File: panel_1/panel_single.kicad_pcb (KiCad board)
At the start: 2 copper layers, 20 x 128.5 mm, 8 parts

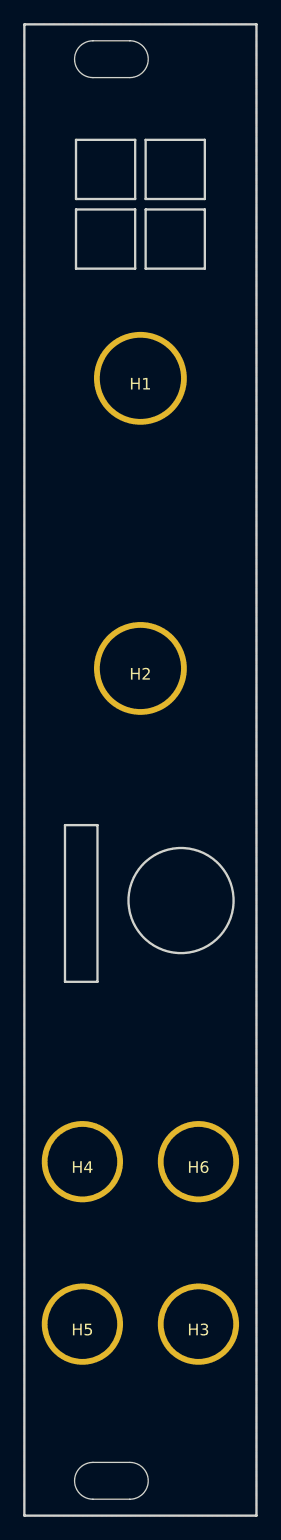
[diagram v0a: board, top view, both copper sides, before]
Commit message: :bug: Fix panel single (better clearance for LEDs & switch)
same
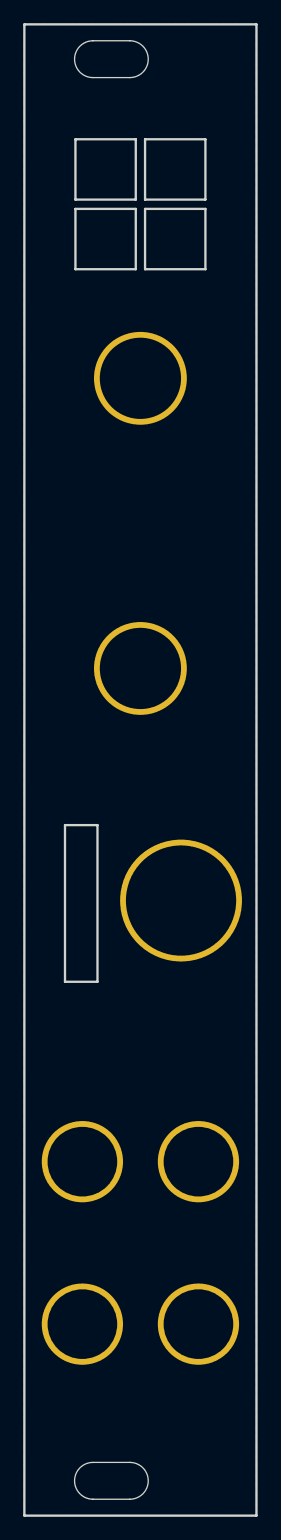
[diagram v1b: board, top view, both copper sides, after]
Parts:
- added H7: MountingHole_Pad, MountingHole:MountingHole_6mm_Pad, F.Cu at (53.5, 105.5)
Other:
- outline, holes or cut-outs redrawn
- board text added: "5mm square holes with .2 mm tolerance"
- board text removed: "5mm square holes with .1 mm tolerance"
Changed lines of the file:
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@@
   (general
     (thickness 1.6)
-    (drawings 85)
+    (drawings 84)
     (tracks 0)
     (zones 0)
-    (modules 8)
+    (modules 9)
     (nets 2)
   )
@@
     (38 B.Mask user)
     (39 F.Mask user)
-    (40 Dwgs.User user)
+    (40 Dwgs.User user hide)
     (41 Cmts.User user)
     (42 Eco1.User user)
@@
     (last_trace_width 0.25)
     (trace_clearance 0.2)
-    (zone_clearance 0.508)
+    (zone_clearance 0)
     (zone_45_only no)
     (trace_min 0.2)
@@
     (mod_text_size 1 1)
     (mod_text_width 0.15)
-    (pad_size 1.524 1.524)
-    (pad_drill 0.762)
+    (pad_size 10.5 10.5)
+    (pad_drill 9.5)
     (pad_to_mask_clearance 0.051)
     (solder_mask_min_width 0.25)
@@
     (add_net GND)
   )
+  (module MountingHole:MountingHole_6mm_Pad (layer F.Cu)
+    (at 53.5 105.5)
+    (descr "Mounting Hole 6mm")
+    (tags "mounting hole 6mm")
+    (attr virtual)
+    (fp_text reference H7 (at 0 -7) (layer F.SilkS) hide
+      (effects (font (size 1 1) (thickness 0.15)))
+    )
+    (fp_text value MountingHole_Pad (at 0 7) (layer F.Fab)
+      (effects (font (size 1 1) (thickness 0.15)))
+    )
+    (fp_circle (center 0 0) (end 6.25 0) (layer F.CrtYd) (width 0.05))
+    (fp_circle (center 0 0) (end 6 0) (layer Cmts.User) (width 0.15))
+    (fp_text user %R (at 22.185 -0.251) (layer F.Fab)
+      (effects (font (size 1 1) (thickness 0.15)))
+    )
+    (pad 1 thru_hole circle (at 0 0) (size 10.5 10.5) (drill 9.5) (layers *.Cu *.Mask)
+      (net 1 GND))
+  )
   (module 4ms-footprints:Rail-mount-slot (layer F.Cu)
     (at 47.5 33)
@@
   (module prok_smd:Alpha_pot_hole_metallized (layer F.Cu)
     (at 50 60.5)
-    (fp_text reference H1 (at 0 0.5) (layer F.SilkS)
+    (fp_text reference H1 (at 0 0.5) (layer F.SilkS) hide
       (effects (font (size 1 1) (thickness 0.15)))
     )
@@
   (module prok_smd:Alpha_pot_hole_metallized (layer F.Cu)
     (at 50 85.5)
-    (fp_text reference H2 (at 0 0.5) (layer F.SilkS)
+    (fp_text reference H2 (at 0 0.5) (layer F.SilkS) hide
       (effects (font (size 1 1) (thickness 0.15)))
     )
@@
   (module prok_smd:thonkiconn_hole_metallized (layer F.Cu)
     (at 55 142)
-    (fp_text reference H3 (at 0 0.5) (layer F.SilkS)
+    (fp_text reference H3 (at 0 0.5) (layer F.SilkS) hide
       (effects (font (size 1 1) (thickness 0.15)))
     )
@@
   (module prok_smd:thonkiconn_hole_metallized (layer F.Cu)
     (at 45 128)
-    (fp_text reference H4 (at 0 0.5) (layer F.SilkS)
+    (fp_text reference H4 (at 0 0.5) (layer F.SilkS) hide
       (effects (font (size 1 1) (thickness 0.15)))
     )
@@
   (module prok_smd:thonkiconn_hole_metallized (layer F.Cu)
     (at 45 142)
-    (fp_text reference H5 (at 0 0.5) (layer F.SilkS)
+    (fp_text reference H5 (at 0 0.5) (layer F.SilkS) hide
       (effects (font (size 1 1) (thickness 0.15)))
     )
@@
   (module prok_smd:thonkiconn_hole_metallized (layer F.Cu)
     (at 55 128)
-    (fp_text reference H6 (at 0 0.5) (layer F.SilkS)
+    (fp_text reference H6 (at 0 0.5) (layer F.SilkS) hide
       (effects (font (size 1 1) (thickness 0.15)))
     )
@@
       (net 1 GND))
   )
-  (gr_text "5mm square holes\nwith .1 mm tolerance" (at 50.2 38.45) (layer Dwgs.User)
+  (gr_line (start 50.5 51) (end 50.5 46) (layer Dwgs.User) (width 0.2))
+  (gr_line (start 44.5 51) (end 44.5 46) (layer Dwgs.User) (width 0.2))
+  (gr_line (start 50.5 45) (end 50.5 40) (layer Dwgs.User) (width 0.2))
+  (gr_line (start 55.5 51) (end 50.5 51) (layer Dwgs.User) (width 0.2))
+  (gr_line (start 49.5 51) (end 44.5 51) (layer Dwgs.User) (width 0.2))
+  (gr_line (start 55.5 45) (end 50.5 45) (layer Dwgs.User) (width 0.2))
+  (gr_line (start 50.5 46) (end 55.5 46) (layer Dwgs.User) (width 0.2))
+  (gr_line (start 44.5 46) (end 49.5 46) (layer Dwgs.User) (width 0.2))
+  (gr_line (start 50.5 40) (end 55.5 40) (layer Dwgs.User) (width 0.2))
+  (gr_line (start 55.5 46) (end 55.5 51) (layer Dwgs.User) (width 0.2))
+  (gr_line (start 49.5 46) (end 49.5 51) (layer Dwgs.User) (width 0.2))
+  (gr_line (start 55.5 40) (end 55.5 45) (layer Dwgs.User) (width 0.2))
+  (gr_line (start 55.6 51.1) (end 50.4 51.1) (layer Edge.Cuts) (width 0.2))
+  (gr_line (start 49.6 51.1) (end 44.4 51.1) (layer Edge.Cuts) (width 0.2))
+  (gr_line (start 55.6 45.1) (end 50.4 45.1) (layer Edge.Cuts) (width 0.2))
+  (gr_line (start 50.4 51.1) (end 50.4 45.9) (layer Edge.Cuts) (width 0.2))
+  (gr_line (start 44.4 51.1) (end 44.4 45.9) (layer Edge.Cuts) (width 0.2))
+  (gr_line (start 50.4 45.1) (end 50.4 39.9) (layer Edge.Cuts) (width 0.2))
+  (gr_line (start 50.4 45.9) (end 55.6 45.9) (layer Edge.Cuts) (width 0.2))
+  (gr_line (start 44.4 45.9) (end 49.6 45.9) (layer Edge.Cuts) (width 0.2))
+  (gr_line (start 50.4 39.9) (end 55.6 39.9) (layer Edge.Cuts) (width 0.2))
+  (gr_line (start 55.6 45.9) (end 55.6 51.1) (layer Edge.Cuts) (width 0.2))
+  (gr_line (start 49.6 45.9) (end 49.6 51.1) (layer Edge.Cuts) (width 0.2))
+  (gr_line (start 55.6 39.9) (end 55.6 45.1) (layer Edge.Cuts) (width 0.2))
+  (gr_text "5mm square holes\nwith .2 mm tolerance" (at 50.2 38.45) (layer Dwgs.User)
     (effects (font (size 0.75 0.75) (thickness 0.1)))
   )
-  (gr_line (start 50.45 51.05) (end 50.45 45.95) (layer Edge.Cuts) (width 0.2))
-  (gr_line (start 55.55 51.05) (end 50.45 51.05) (layer Edge.Cuts) (width 0.2))
-  (gr_line (start 55.55 45.95) (end 55.55 51.05) (layer Edge.Cuts) (width 0.2))
-  (gr_line (start 50.45 45.95) (end 55.55 45.95) (layer Edge.Cuts) (width 0.2))
-  (gr_line (start 44.45 51.05) (end 44.45 45.95) (layer Edge.Cuts) (width 0.2))
-  (gr_line (start 49.55 51.05) (end 44.45 51.05) (layer Edge.Cuts) (width 0.2))
-  (gr_line (start 49.55 45.95) (end 49.55 51.05) (layer Edge.Cuts) (width 0.2))
-  (gr_line (start 44.45 45.95) (end 49.55 45.95) (layer Edge.Cuts) (width 0.2))
-  (gr_line (start 50.45 45.05) (end 50.45 39.95) (layer Edge.Cuts) (width 0.2))
-  (gr_line (start 55.55 45.05) (end 50.45 45.05) (layer Edge.Cuts) (width 0.2))
-  (gr_line (start 55.55 39.95) (end 55.55 45.05) (layer Edge.Cuts) (width 0.2))
-  (gr_line (start 50.45 39.95) (end 55.55 39.95) (layer Edge.Cuts) (width 0.2))
-  (gr_line (start 44.45 45.05) (end 44.45 39.95) (layer Edge.Cuts) (width 0.2))
-  (gr_line (start 49.55 45.05) (end 44.45 45.05) (layer Edge.Cuts) (width 0.2))
-  (gr_line (start 49.55 39.95) (end 49.55 45.05) (layer Edge.Cuts) (width 0.2))
-  (gr_line (start 44.45 39.95) (end 49.55 39.95) (layer Edge.Cuts) (width 0.2))
+  (gr_line (start 44.4 45.1) (end 44.4 39.9) (layer Edge.Cuts) (width 0.2))
+  (gr_line (start 49.6 45.1) (end 44.4 45.1) (layer Edge.Cuts) (width 0.2))
+  (gr_line (start 49.6 39.9) (end 49.6 45.1) (layer Edge.Cuts) (width 0.2))
+  (gr_line (start 44.4 39.9) (end 49.6 39.9) (layer Edge.Cuts) (width 0.2))
   (gr_circle (center 55 136) (end 56 136) (layer F.Mask) (width 0.2))
   (gr_line (start 44 137) (end 46 137) (layer F.Mask) (width 0.2))
@@
     (arrow2b (pts (xy 44.5 64) (xy 45.086421 65.126504)))
   )
-  (gr_circle (center 53.5 105.5) (end 58 105) (layer Edge.Cuts) (width 0.2))
   (dimension 9 (width 0.3) (layer Dwgs.User)
     (gr_text "9,000 mm" (at 53.5 117.6) (layer Dwgs.User)
@@
     (arrow2b (pts (xy 35.5 30) (xy 36.086421 31.126504)))
   )
-  (gr_line (start 55.5 45) (end 50.5 45) (layer Dwgs.User) (width 0.2))
-  (gr_line (start 55.5 40) (end 55.5 45) (layer Dwgs.User) (width 0.2))
-  (gr_line (start 50.5 40) (end 55.5 40) (layer Dwgs.User) (width 0.2))
-  (gr_line (start 50.5 45) (end 50.5 40) (layer Dwgs.User) (width 0.2))
   (gr_line (start 49.5 40) (end 49.5 45) (layer Dwgs.User) (width 0.2))
   (gr_line (start 44.5 40) (end 49.5 40) (layer Dwgs.User) (width 0.2))
   (gr_line (start 44.5 45) (end 44.5 40) (layer Dwgs.User) (width 0.2))
   (gr_line (start 49.5 45) (end 44.5 45) (layer Dwgs.User) (width 0.2))
-  (gr_line (start 49.5 51) (end 49.5 46) (layer Dwgs.User) (width 0.2))
-  (gr_line (start 44.5 51) (end 49.5 51) (layer Dwgs.User) (width 0.2))
-  (gr_line (start 44.5 46) (end 44.5 51) (layer Dwgs.User) (width 0.2))
-  (gr_line (start 49.5 46) (end 44.5 46) (layer Dwgs.User) (width 0.2))
-  (gr_line (start 50.5 46) (end 50.5 51) (layer Dwgs.User) (width 0.2))
-  (gr_line (start 55.5 46) (end 50.5 46) (layer Dwgs.User) (width 0.2))
-  (gr_line (start 55.5 51) (end 55.5 46) (layer Dwgs.User) (width 0.2))
-  (gr_line (start 50.5 51) (end 55.5 51) (layer Dwgs.User) (width 0.2))
   (dimension 5 (width 0.3) (layer Dwgs.User)
     (gr_text "5,000 mm" (at 65.1 48.5 270) (layer Dwgs.User)
@@
   )
   (zone (net 1) (net_name GND) (layer F.Cu) (hatch edge 0.508)
-    (connect_pads (clearance 0.508))
+    (connect_pads yes (clearance 0))
     (min_thickness 0.254)
     (fill yes (arc_segments 32) (thermal_gap 0.508) (thermal_bridge_width 0.508))
@@
   )
   (zone (net 1) (net_name GND) (layer B.Cu) (hatch edge 0.508)
-    (connect_pads (clearance 0.508))
+    (connect_pads yes (clearance 0))
     (min_thickness 0.254)
     (fill yes (arc_segments 32) (thermal_gap 0.508) (thermal_bridge_width 0.508))

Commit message: :sparkles: update panels
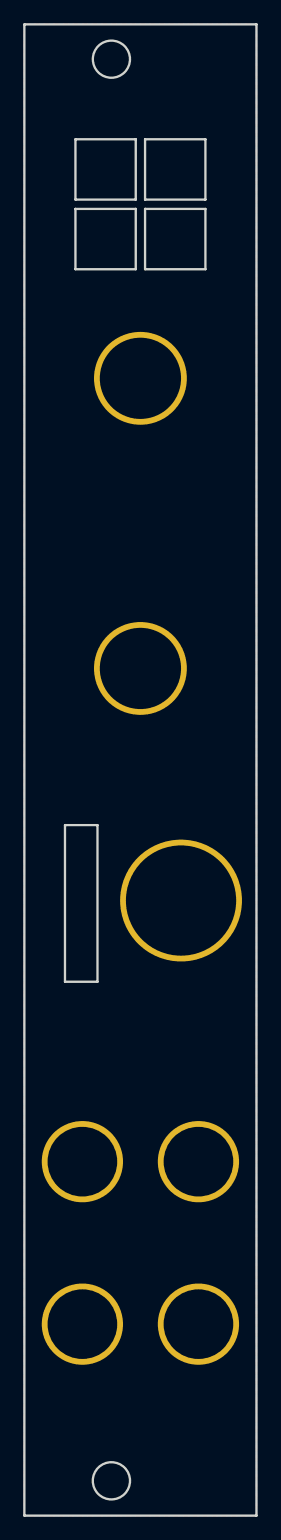
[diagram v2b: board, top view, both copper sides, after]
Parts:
- removed REF** (x2): Rail-mount-slot, 4ms-footprints:Rail-mount-slot
- added G***: LOGO, NN_Footprints:nebularnoise_logo, B.Cu at (49.6, 149.1)
- added G***: LOGO, NN_Footprints:quad1, F.Cu at (54.8, 33.0)
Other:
- outline, holes or cut-outs redrawn
- board text added: "QUADRANTS_PANEL v1.0"
- board text added: "github.com/nebularnoise/quadrants"
